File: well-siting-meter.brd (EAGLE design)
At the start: 93.8 x 65.9 mm, 47 parts, among them J2 7805, T1 MOSFET-NCHANNELFQP30N06L, U1 LCD-16X2NOHOLES, U2 ARDUINO_PRO_MINI, U3 EC2, U4 EC2, U5 AD623, U6 AD623, U7 MAX1771

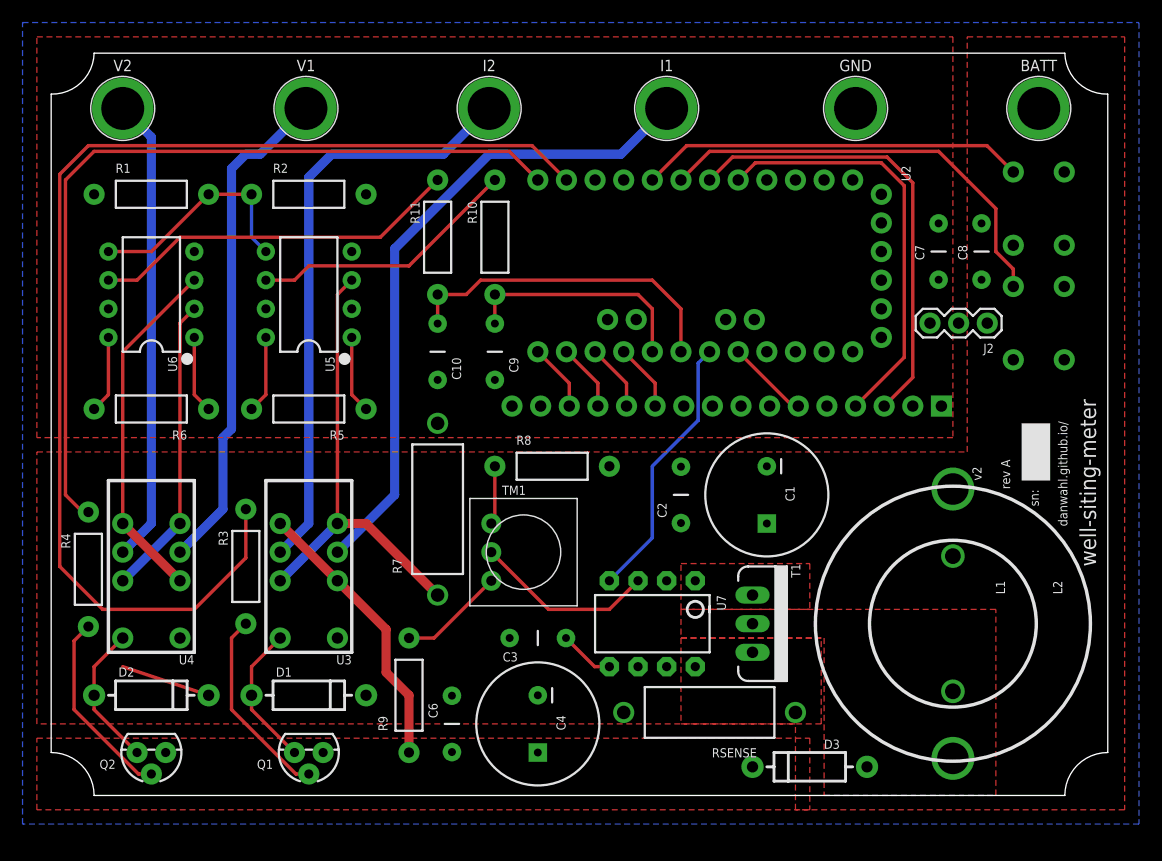
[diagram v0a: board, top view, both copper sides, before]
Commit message: start of rev B updates (added relay, AD629, fuse)
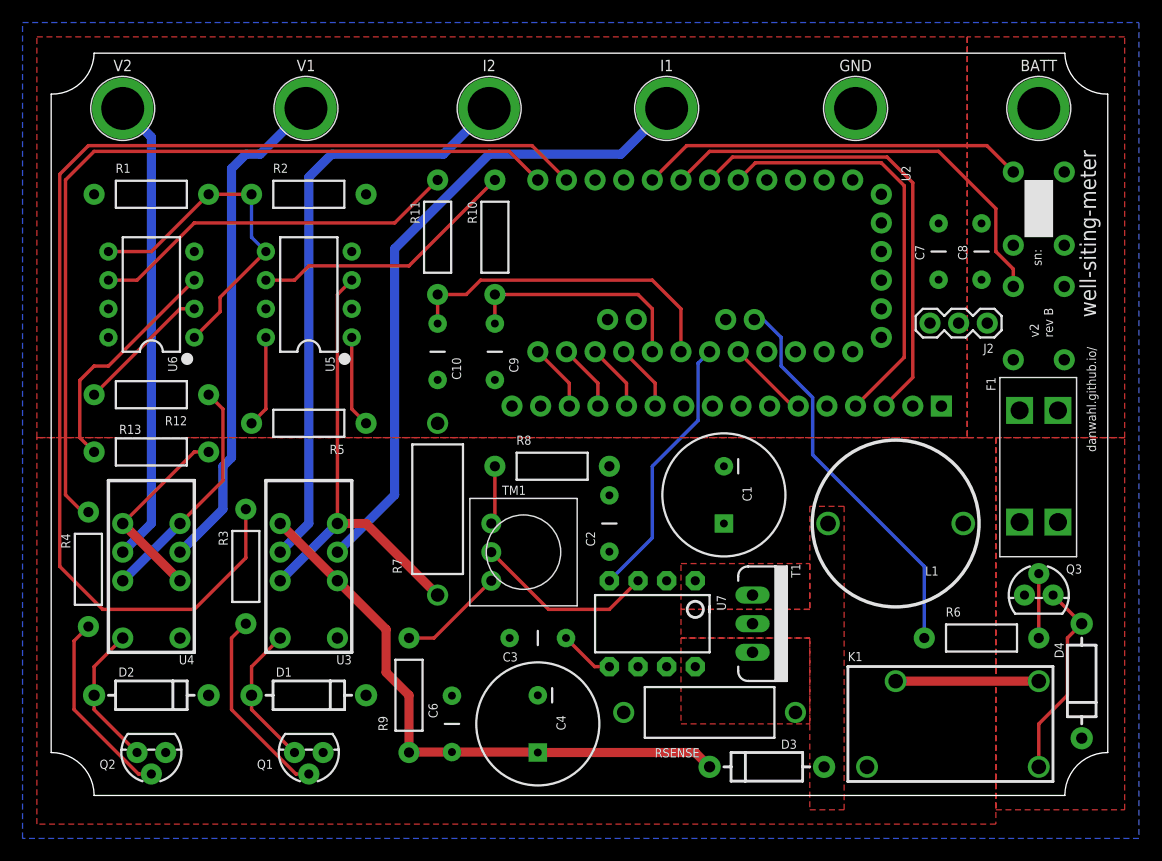
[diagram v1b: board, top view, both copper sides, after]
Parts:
- removed L2: 47uH, murata1400:MURATA1400
- added D4: (no value), SparkFun-DiscreteSemi:DIODE-1N4001
- added F1: 3568, keystone:3568
- added K1: (no value), oje:OJ-SH-124LMH
- added Q3: (no value), SparkFun-DiscreteSemi:TO-92
- added R12, R13: 10K, SparkFun-Passives:AXIAL-0.4
- R6: value 100K -> 392R
- U6: value AD623 -> AD629
- moved R6 76.4 mm to (82.5, 14.0), turned to 0 degrees
- moved L1 10.2 mm to (74.9, 24.1), turned to 180 degrees
- moved C2 6.84 mm to (49.5, 24.1)
- moved C1 3.81 mm to (59.7, 26.7)
- moved D3 3.81 mm to (63.5, 2.54)
- moved R5 1.27 mm to (22.9, 33.0)
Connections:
- removed net N$26: R6.P$1, U6.1
- removed net N$27: R6.P$2, U6.8
- new net BATT: C8.1, F1.1, F1.2, J2.1, J7.P$1
- new net FUSE: D4.C, F1.3, F1.4, K1.1, K1.2
- new net N$13: R12.P$2, U6.2
- new net N$16: R13.P$2, U6.3
- new net N$17: D4.A, K1.4, Q3.3
- new net N$18: Q3.2, R6.P$2
- new net RSW: R6.P$1, U2.A5
- net GND: now also Q3.1
- net N$9: no longer L2.P$2
- net V+: now also R13.P$1; no longer U6.3
- net V-: now also R12.P$1; no longer U6.2
- net VREF: now also U6.1
- net V_BATT: now also K1.3; no longer C8.1, J2.1, J7.P$1, L2.P$1
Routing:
- net RSW: track 0.00 -> 35.0 mm
- net VIN: track 25.1 -> 52.3 mm
- net N$16: track 0.00 -> 20.7 mm
- net N$17: track 0.00 -> 17.9 mm
- net V+: track 31.4 -> 17.4 mm
- net FUSE: track 0.00 -> 12.7 mm
- net N$13: track 0.00 -> 12.0 mm
- net VREF: track 20.4 -> 30.7 mm
- net V_BATT: track 8.03 -> 0.00 mm
- net N$26: track 6.88 -> 0.00 mm
- net N$27: track 6.88 -> 0.00 mm
- net V-: track 26.8 -> 20.7 mm
- net N$18: track 0.00 -> 5.71 mm
- net N$25: track 6.88 -> 8.15 mm
- net N$24: track 6.88 -> 8.15 mm
- added copper zone on layer 1, net BATT
- added copper zone on layer 1, net FUSE
- removed copper zone on layer 1, net VIN
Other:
- board text added: "rev B"
- board text removed: "rev A"

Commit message: rev B updates (AD629, fuse holder, power relay)
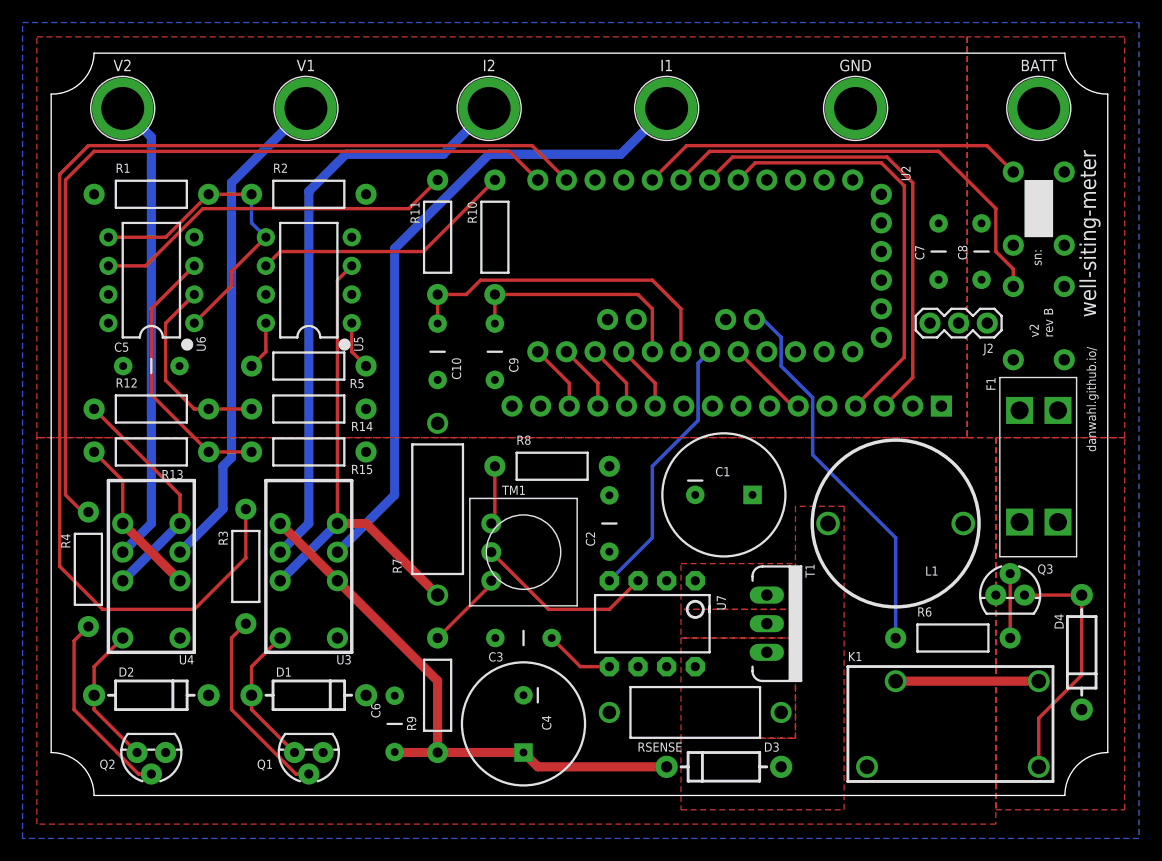
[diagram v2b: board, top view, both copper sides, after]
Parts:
- added C5: 0.1uf, SparkFun-Passives:CAP-PTH-5MM
- added R14, R15: 44.2K, SparkFun-Passives:AXIAL-0.4
- moved C6 5.08 mm to (30.5, 6.35)
- moved R5 5.08 mm to (22.9, 38.1)
- moved D3 3.81 mm to (59.7, 2.54)
- moved D4 2.54 mm to (91.4, 12.7)
- moved R9 2.54 mm to (34.3, 8.89)
- moved Q3 2.54 mm to (85.1, 17.8)
- moved R6 2.54 mm to (80.0, 14.0)
- moved C3 1.27 mm to (41.9, 14.0)
- moved C4 1.27 mm to (41.9, 6.35)
- moved R12 1.27 mm to (8.89, 34.3), turned to 0 degrees
- moved RSENSE 1.27 mm to (57.1, 7.37)
- moved T1 1.27 mm to (63.5, 15.2)
- moved U5 1.27 mm to (22.9, 45.7)
- moved U6 1.27 mm to (8.89, 45.7)
- turned C1 to 0 degrees
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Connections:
- net 5V: now also C5.1
- net GND: now also C5.2, R14.P$1, R15.P$1
- net N$13: now also R14.P$2
- net N$16: now also R15.P$2
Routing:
- net N$13: track 12.0 -> 17.3 mm
- net N$17: track 17.9 -> 21.9 mm
- net N$25: track 8.15 -> 4.34 mm
- net N$24: track 8.15 -> 4.34 mm
- net N$16: track 20.7 -> 24.0 mm
- net V+: track 17.4 -> 14.6 mm
- net N$6: track 9.41 -> 7.05 mm
- net VREF: track 30.7 -> 28.9 mm
- net VIN: track 52.3 -> 50.8 mm
- net N$7: track 4.90 -> 6.17 mm
- net IRET: track 40.8 -> 42.1 mm
- net RSW: track 35.0 -> 33.9 mm
- net V1: track 44.7 -> 44.0 mm
- net I2: track 52.9 -> 52.1 mm
- net N$14: track 32.9 -> 32.4 mm
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
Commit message: adding ic1 for 2.5 vref
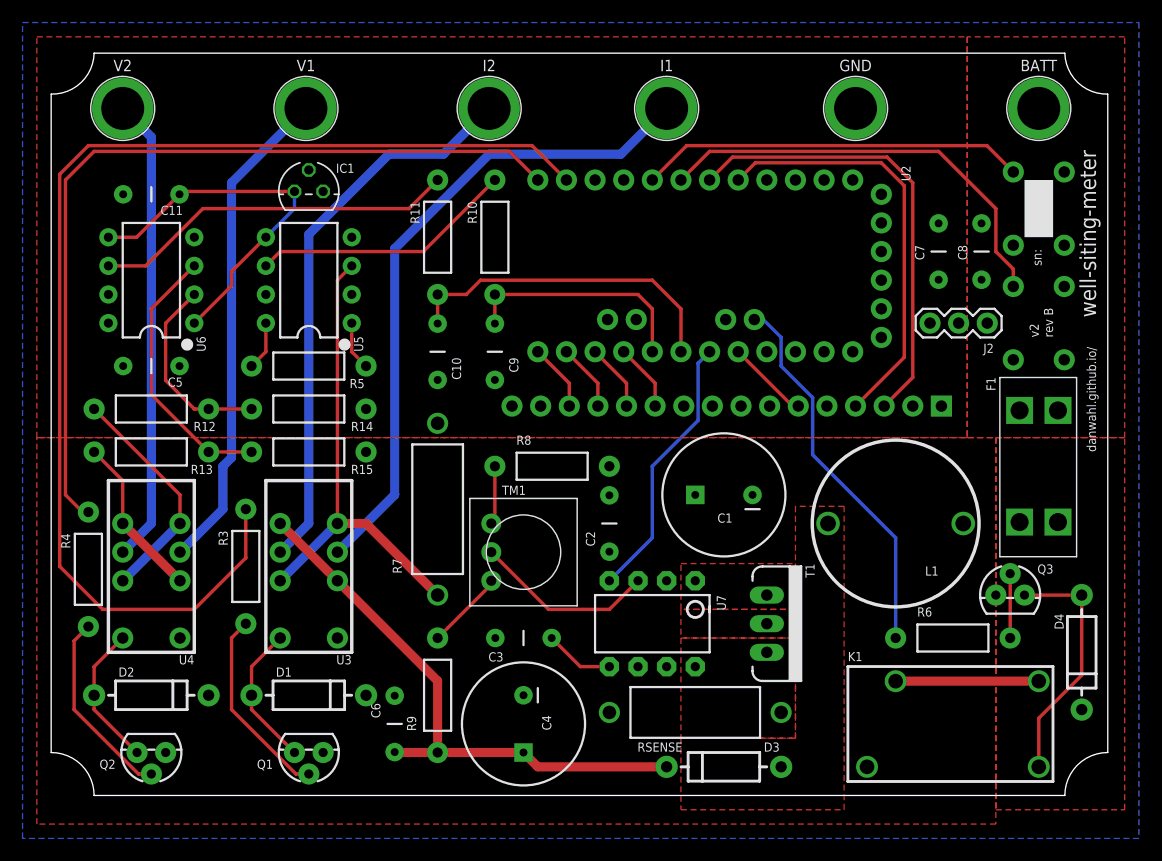
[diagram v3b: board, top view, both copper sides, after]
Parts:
- removed R1, R2: 10K, SparkFun-Passives:AXIAL-0.4
- added C11: 0.1uf, SparkFun-Passives:CAP-PTH-5MM
- added IC1: LM336LP, linear:TO92
- turned C1 to 180 degrees
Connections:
- net 5V: now also IC1.2; no longer R1.P$1
- net GND: now also C11.2, IC1.3; no longer R2.P$2
- net VREF: now also C11.1, IC1.1; no longer R1.P$2, R2.P$1
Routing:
- net VREF: track 28.9 -> 33.6 mm
- net I2: track 52.1 -> 49.9 mm
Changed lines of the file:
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@@
 <attribute name="VALUE" x="5.969" y="8.382" size="1.016" layer="21" ratio="12"/>
-</element>
-<element name="R1" library="SparkFun-Passives" package="AXIAL-0.4" value="10K" x="8.89" y="53.34" smashed="yes">
-<attribute name="NAME" x="5.715" y="55.245" size="0.8128" layer="25" font="vector" ratio="10"/>
-<attribute name="PN" value="10.0KXBK-ND" x="8.89" y="53.34" size="1.778" layer="27" display="off"/>
-<attribute name="VALUE" x="6.604" y="52.959" size="0.8128" layer="27" font="vector" ratio="10"/>
-</element>
-<element name="R2" library="SparkFun-Passives" package="AXIAL-0.4" value="10K" x="22.86" y="53.34" smashed="yes">
-<attribute name="NAME" x="19.685" y="55.245" size="0.8128" layer="25" font="vector" ratio="10"/>
-<attribute name="PN" value="10.0KXBK-ND" x="22.86" y="53.34" size="1.778" layer="27" display="off"/>
-<attribute name="VALUE" x="20.574" y="52.959" size="0.8128" layer="27" font="vector" ratio="10"/>
 </element>
 <element name="R3" library="SparkFun-Passives" package="AXIAL-0.4" value="392R" x="17.272" y="20.32" smashed="yes" rot="R270">
@@
 <attribute name="PROD_ID" value=" SWCH-08441" x="87.63" y="52.07" size="1.778" layer="28" rot="MR270" display="off"/>
 </element>
-<element name="C1" library="SparkFun-Passives" package="CPOL-RADIAL-1000UF-25V" value="100uF" x="59.69" y="26.67" smashed="yes">
-<attribute name="NAME" x="58.928" y="28.321" size="0.8128" layer="25" font="vector"/>
-<attribute name="PN" value="1572-1306-ND" x="59.69" y="26.67" size="1.778" layer="27" display="off"/>
-<attribute name="VALUE" x="57.023" y="23.368" size="0.8128" layer="27" font="vector"/>
+<element name="C1" library="SparkFun-Passives" package="CPOL-RADIAL-1000UF-25V" value="100uF" x="59.69" y="26.67" smashed="yes" rot="R180">
+<attribute name="NAME" x="60.452" y="25.019" size="0.8128" layer="25" font="vector" rot="R180"/>
+<attribute name="PN" value="1572-1306-ND" x="59.69" y="26.67" size="1.778" layer="27" rot="R180" display="off"/>
+<attribute name="VALUE" x="62.357" y="29.972" size="0.8128" layer="27" font="vector" rot="R180"/>
 </element>
 <element name="C2" library="SparkFun-Passives" package="CAP-PTH-5MM" value="0.1uf" x="49.53" y="24.13" smashed="yes" rot="R90">
@@
 </element>
 <element name="R12" library="SparkFun-Passives" package="AXIAL-0.4" value="10K" x="8.89" y="34.29" smashed="yes">
-<attribute name="NAME" x="5.715" y="36.195" size="0.8128" layer="25" font="vector" ratio="10"/>
+<attribute name="NAME" x="14.605" y="33.147" size="0.8128" layer="25" font="vector" ratio="10" align="top-right"/>
 <attribute name="PN" value="10.0KXBK-ND" x="8.89" y="34.29" size="1.778" layer="27" display="off"/>
 <attribute name="VALUE" x="6.604" y="33.909" size="0.8128" layer="27" font="vector" ratio="10"/>
 </element>
 <element name="R13" library="SparkFun-Passives" package="AXIAL-0.4" value="10K" x="8.89" y="30.48" smashed="yes">
-<attribute name="NAME" x="9.779" y="28.067" size="0.8128" layer="25" font="vector" ratio="10"/>
+<attribute name="NAME" x="14.351" y="29.337" size="0.8128" layer="25" font="vector" ratio="10" align="top-right"/>
 <attribute name="PN" value="10.0KXBK-ND" x="8.89" y="30.48" size="1.778" layer="27" display="off"/>
 <attribute name="VALUE" x="6.604" y="30.099" size="0.8128" layer="27" font="vector" ratio="10"/>
@@
 </element>
 <element name="C5" library="SparkFun-Passives" package="CAP-PTH-5MM" value="0.1uf" x="8.89" y="38.1" smashed="yes">
-<attribute name="NAME" x="5.588" y="39.37" size="0.8128" layer="25" font="vector" ratio="10"/>
+<attribute name="NAME" x="11.684" y="37.084" size="0.8128" layer="25" font="vector" ratio="10" align="top-right"/>
 <attribute name="PN" value="BC2665CT-ND" x="8.89" y="38.1" size="0.8128" layer="27" font="vector" display="off"/>
-<attribute name="VALUE" x="7.874" y="39.116" size="0.8128" layer="27" font="vector" ratio="10"/>
+<attribute name="VALUE" x="6.604" y="39.116" size="0.8128" layer="27" font="vector" ratio="10"/>
+</element>
+<element name="IC1" library="linear" library_urn="urn:adsk.eagle:library:262" package="TO92" package3d_urn="urn:adsk.eagle:package:16416/2" value="LM336LP" x="22.86" y="53.594" smashed="yes">
+<attribute name="NAME" x="25.273" y="55.245" size="0.8128" layer="25" font="vector" ratio="10"/>
+<attribute name="VALUE" x="25.781" y="52.324" size="0.8128" layer="27" font="vector" ratio="10"/>
+</element>
+<element name="C11" library="SparkFun-Passives" package="CAP-PTH-5MM" value="0.1uf" x="8.89" y="53.34" smashed="yes" rot="R180">
+<attribute name="NAME" x="11.684" y="52.324" size="0.8128" layer="25" font="vector" ratio="10" rot="R180"/>
+<attribute name="PN" value="BC2665CT-ND" x="8.89" y="53.34" size="0.8128" layer="27" font="vector" ratio="10" rot="R180" display="off"/>
+<attribute name="VALUE" x="9.906" y="54.864" size="0.8128" layer="27" font="vector" ratio="10" rot="R180"/>
 </element>
 </elements>
@@
 <contactref element="U5" pad="4"/>
 <contactref element="U6" pad="4"/>
-<contactref element="R2" pad="P$2"/>
 <contactref element="R7" pad="P$2"/>
 <contactref element="J2" pad="2"/>
@@
 <contactref element="R14" pad="P$1"/>
 <contactref element="C5" pad="2"/>
+<contactref element="IC1" pad="3"/>
+<contactref element="C11" pad="2"/>
 </signal>
 <signal name="5V">
@@
 <contactref element="U5" pad="7"/>
 <contactref element="U6" pad="7"/>
-<contactref element="R1" pad="P$1"/>
 <contactref element="J2" pad="3"/>
 <contactref element="C7" pad="1"/>
@@
 </polygon>
 <contactref element="C5" pad="1"/>
+<contactref element="IC1" pad="2"/>
 </signal>
 <signal name="N$1">
@@
 <contactref element="U3" pad="4"/>
 <contactref element="J10" pad="P$1"/>
-<wire x1="22.86" y1="53.594" x2="22.86" y2="24.13" width="0.8128" layer="16"/>
+<wire x1="22.86" y1="49.784" x2="22.86" y2="24.13" width="0.8128" layer="16"/>
 <wire x1="20.32" y1="21.59" x2="22.86" y2="24.13" width="0.8128" layer="16"/>
-<wire x1="22.86" y1="53.594" x2="26.162" y2="56.896" width="0.8128" layer="16"/>
-<wire x1="26.162" y1="56.896" x2="34.798" y2="56.896" width="0.8128" layer="16"/>
-<wire x1="34.798" y1="56.896" x2="38.862" y2="60.96" width="0.8128" layer="16"/>
+<wire x1="38.862" y1="60.96" x2="34.798" y2="56.896" width="0.8128" layer="16"/>
+<wire x1="34.798" y1="56.896" x2="29.972" y2="56.896" width="0.8128" layer="16"/>
+<wire x1="29.972" y1="56.896" x2="22.86" y2="49.784" width="0.8128" layer="16"/>
 </signal>
 <signal name="IRET">
@@
 <contactref element="J12" pad="P$1"/>
 <wire x1="6.35" y1="60.96" x2="8.89" y2="58.42" width="0.8128" layer="16"/>
-<wire x1="8.89" y1="58.42" x2="8.89" y2="24.13" width="0.8128" layer="16"/>
+<wire x1="8.89" y1="58.42" x2="8.89" y2="49.53" width="0.8128" layer="16"/>
+<wire x1="8.89" y1="49.53" x2="8.89" y2="24.13" width="0.8128" layer="16"/>
 <wire x1="6.35" y1="21.59" x2="8.89" y2="24.13" width="0.8128" layer="16"/>
 </signal>
@@
 <wire x1="11.43" y1="21.59" x2="15.24" y2="25.4" width="0.8128" layer="16"/>
 <wire x1="15.24" y1="25.4" x2="15.24" y2="29.21" width="0.8128" layer="16"/>
-<wire x1="15.24" y1="29.21" x2="16.002" y2="29.972" width="0.8128" layer="16"/>
-<wire x1="16.002" y1="29.972" x2="16.002" y2="54.356" width="0.8128" layer="16"/>
-<wire x1="16.002" y1="54.356" x2="22.606" y2="60.96" width="0.8128" layer="16"/>
+<wire x1="16.002" y1="29.972" x2="15.24" y2="29.21" width="0.8128" layer="16"/>
+<wire x1="22.606" y1="60.96" x2="16.002" y2="54.356" width="0.8128" layer="16"/>
+<wire x1="16.002" y1="54.356" x2="16.002" y2="29.972" width="0.8128" layer="16"/>
 </signal>
 <signal name="VREF">
-<contactref element="R1" pad="P$2"/>
-<contactref element="R2" pad="P$1"/>
 <contactref element="U5" pad="5"/>
 <contactref element="U6" pad="5"/>
-<wire x1="13.97" y1="53.34" x2="17.78" y2="53.34" width="0.3048" layer="1"/>
-<wire x1="17.78" y1="53.34" x2="17.78" y2="50.8" width="0.3048" layer="16"/>
-<wire x1="17.78" y1="50.8" x2="19.05" y2="49.53" width="0.3048" layer="16"/>
-<wire x1="10.16" y1="49.53" x2="13.97" y2="53.34" width="0.3048" layer="1"/>
-<wire x1="5.08" y1="49.53" x2="10.16" y2="49.53" width="0.3048" layer="1"/>
 <contactref element="U6" pad="1"/>
 <wire x1="19.05" y1="49.53" x2="16.002" y2="46.482" width="0.3048" layer="1"/>
 <wire x1="16.002" y1="46.482" x2="16.002" y2="45.212" width="0.3048" layer="1"/>
 <wire x1="16.002" y1="45.212" x2="12.7" y2="41.91" width="0.3048" layer="1"/>
+<contactref element="IC1" pad="1"/>
+<wire x1="19.05" y1="49.53" x2="21.59" y2="52.07" width="0.3048" layer="16"/>
+<wire x1="21.59" y1="52.07" x2="21.59" y2="53.594" width="0.3048" layer="16"/>
+<contactref element="C11" pad="1"/>
+<wire x1="11.39" y1="53.34" x2="7.58" y2="49.53" width="0.3048" layer="1"/>
+<wire x1="7.58" y1="49.53" x2="5.08" y2="49.53" width="0.3048" layer="1"/>
+<wire x1="11.39" y1="53.34" x2="11.644" y2="53.594" width="0.3048" layer="1"/>
+<wire x1="11.644" y1="53.594" x2="21.59" y2="53.594" width="0.3048" layer="1"/>
 </signal>
 <signal name="V_BATT">
@@
 </board>
 </drawing>
+<compatibility>
+<note version="8.2" severity="warning">
+Since Version 8.2, EAGLE supports online libraries. The ids
+of those online libraries will not be understood (or retained)
+with this version.
+</note>
+<note version="8.3" severity="warning">
+Since Version 8.3, EAGLE supports URNs for individual library
+assets (packages, symbols, and devices). The URNs of those assets
+will not be understood (or retained) with this version.
+</note>
+<note version="8.3" severity="warning">
+Since Version 8.3, EAGLE supports the association of 3D packages
+with devices in libraries, schematics, and board files. Those 3D
+packages will not be understood (or retained) with this version.
+</note>
+</compatibility>
 </eagle>
